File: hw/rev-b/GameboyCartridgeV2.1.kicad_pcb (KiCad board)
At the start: 6 copper layers, 52.8 x 61.2 mm, 148 parts, among them J1 USB_C_Receptacle_USB2.0, J2 Micro_SD_Card_Det2, J4 Conn_01x06, J5 CartBus, Q1 CJ2302, Q101 SIA975DJ-T1-GE3, Q102 2N7002, SW1 SW_Push, SW2 SW_Push, U1 USBLC6-2P6, U101 TPS2116DRLR, U102 TPS2553DBVR, U103 TPS63802DLAR, U104 ESP32-C3-MINI-1U-N4, U105 SN74LVC1G125DBVR, U106 SN74LVC3G34DCTR, U107 CH334P, U108 TLV3012BIDBVR, U109 TLV431BIDBZR, U2 W25Q16JVSSIQ, U3 RP2350_80QFN, U4 W956A8MBYA5I, U5 MCP79510, U6 AP2112K-3.3, U7 TXB0108PW, Y1 12MHz, Y101 12MHz 10pF 10ppm, Y2 32.768kHz

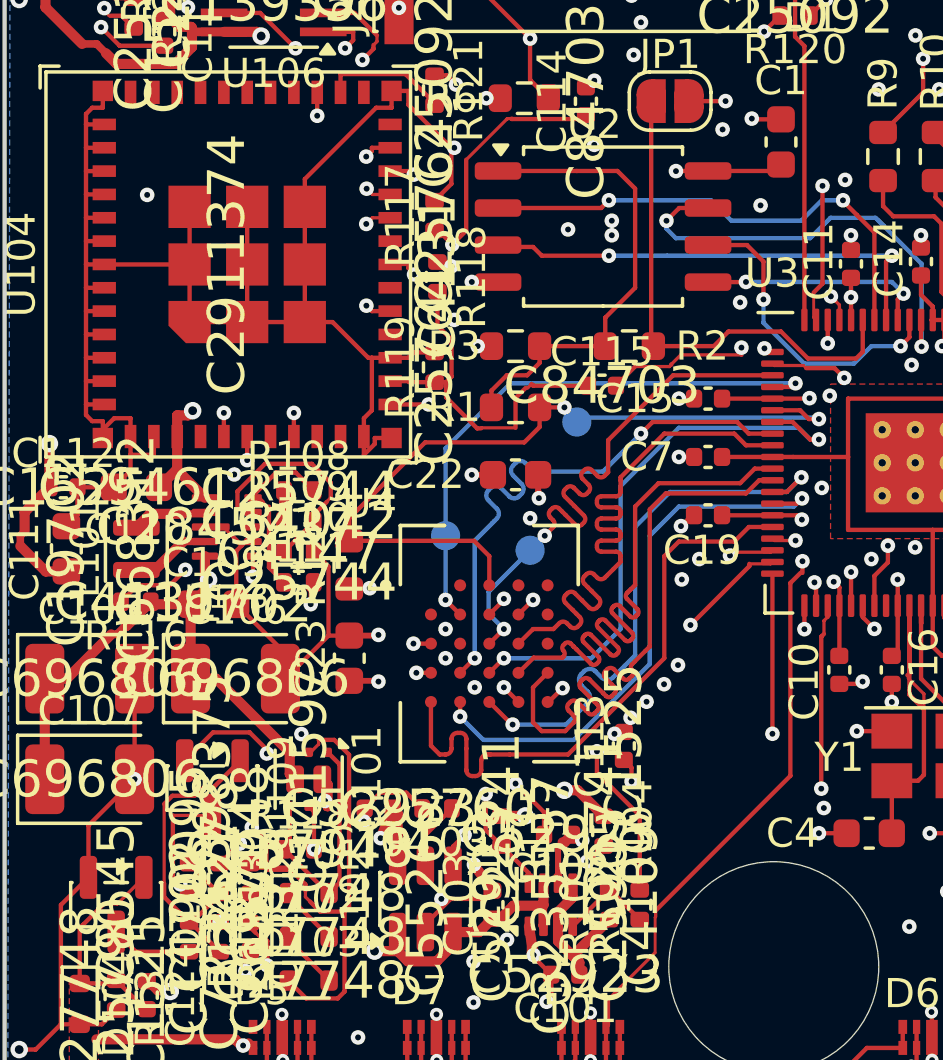
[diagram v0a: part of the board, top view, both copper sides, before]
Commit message: routing WIP: FB/PG resistor block re-arranged, USB_PWR_ST moved to ESP IO5 (pin 19), ADC_VCC divider moved to the VCC source; 5 open
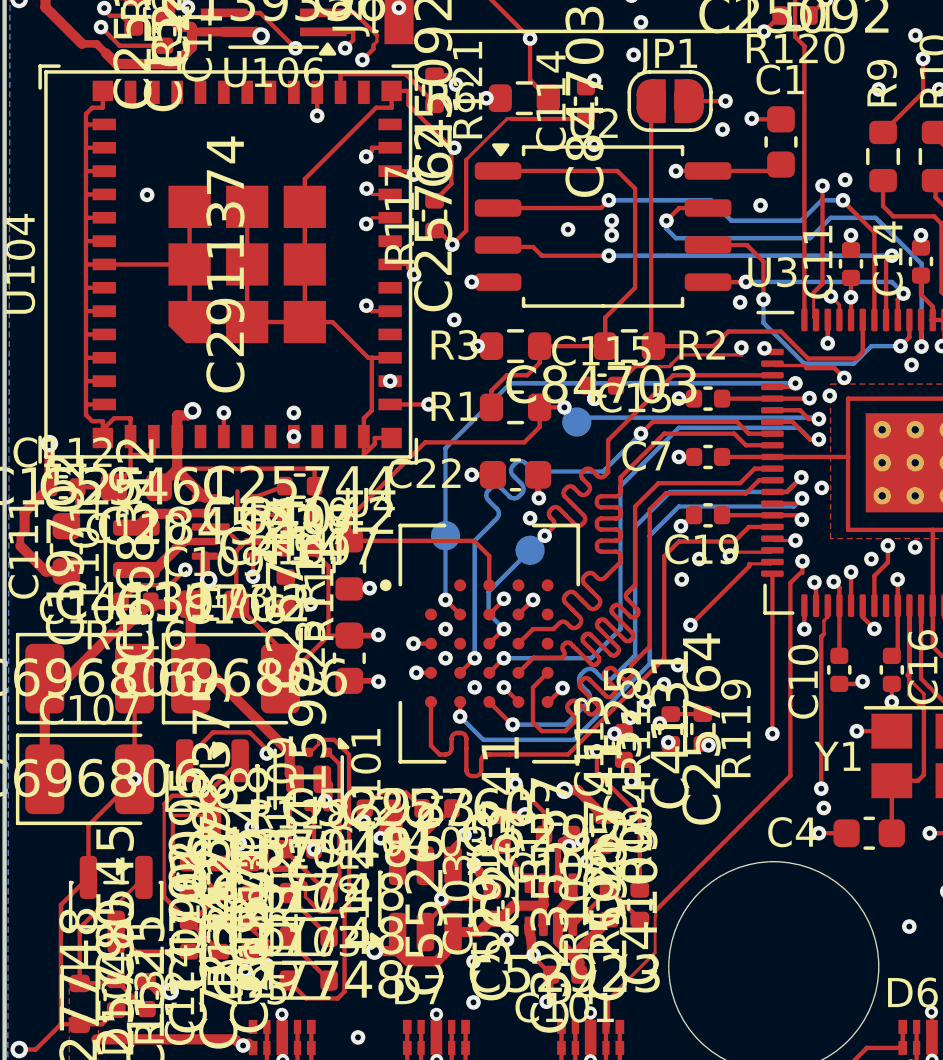
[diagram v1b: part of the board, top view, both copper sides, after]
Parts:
- moved R118 17.4 mm to (136.2, 99.9), turned to 90 degrees
- moved R119 15.4 mm to (137.3, 99.9), turned to -90 degrees
- moved R111 0.55 mm to (123.0, 95.2), turned to -90 degrees
- moved R108 0.15 mm to (123.5, 91.6), turned to 180 degrees
- moved R109 0.15 mm to (123.5, 92.7), turned to 180 degrees
- moved R110 0.15 mm to (123.5, 93.7)
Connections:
- U104 pad 19: unconnected-(U104-IO5-Pad19) -> /Radio/USB_PWR_ST
- U104 pad 6: /Radio/USB_PWR_ST -> unconnected-(U104-IO3-Pad6)
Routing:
- net VCC: track 77.6 -> 44.0 mm, vias 11 -> 10
- net /Radio/USB_PWR_ST: track 20.1 -> 1.58 mm, vias 2 -> 0
- net /Radio/ADC_VCC: track 12.4 -> 24.6 mm, vias 0 -> 4
- net /Radio/+3V3_RF: track 81.5 -> 86.8 mm
- net /Radio/RF_PG: track 6.22 -> 1.16 mm
- net /Radio/RF_FB: track 8.06 -> 3.28 mm
- net /Radio/ESP_EN: track 22.8 -> 21.2 mm
- net GND: track 229.7 -> 231.0 mm, vias 210 -> 212

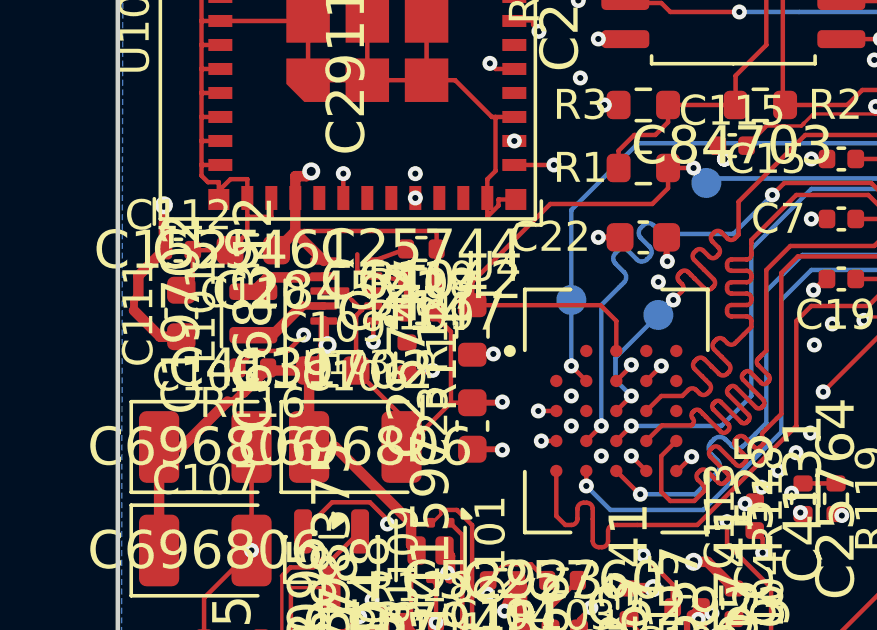
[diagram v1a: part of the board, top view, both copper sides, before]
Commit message: gate S1: full-system simulation with a Game Boy ROM (Peanut-GB + mailbox + RP2350/ESP models + shipped power manager + power plant), all pass; routing WIP; logbook
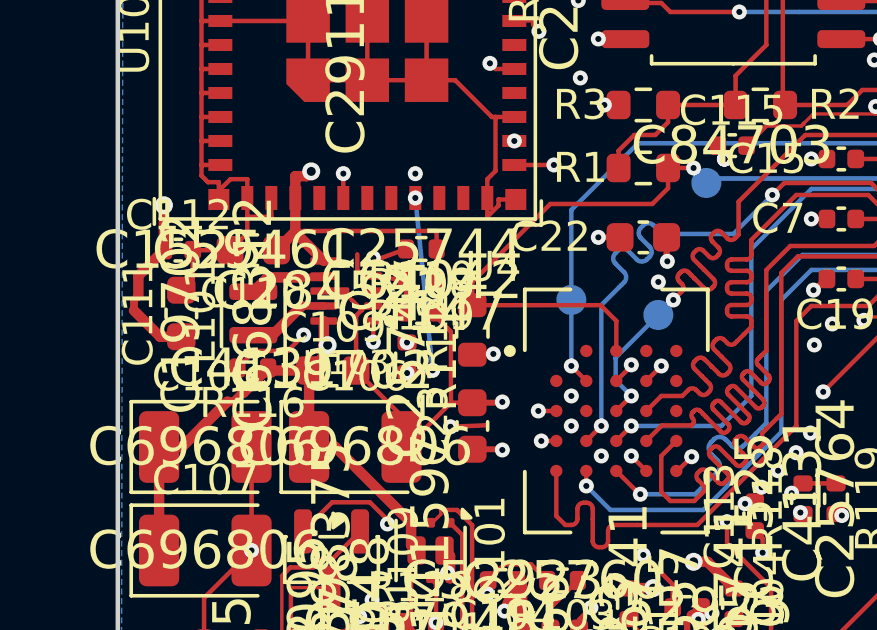
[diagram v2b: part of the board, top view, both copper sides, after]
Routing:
- net VRES: track 70.1 -> 59.7 mm
- net /Radio/RF_EN: track 34.0 -> 29.8 mm
- net /Radio/RF_PG: track 1.16 -> 4.54 mm, vias 0 -> 2
- net /Radio/ADC_VRES: track 29.1 -> 32.4 mm
- net /Radio/ESP_EN: track 21.2 -> 22.0 mm, vias 3 -> 5
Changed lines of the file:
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@@
-	)
-	(segment
-		(start 121.9 94.7042)
-		(end 123.6608 94.7042)
-		(width 0.15)
-		(layer "In2.Cu")
-		(net "/Radio/RF_EN")
 	)
 	(segment
@@
 	)
 	(segment
-		(start 123.6608 94.7042)
-		(end 125.4233 96.4667)
-		(width 0.15)
-		(layer "In2.Cu")
-		(net "/Radio/RF_EN")
-	)
-	(segment
 		(start 121.3662 92.3504)
 		(end 121.3662 91.7783)
@@
 		(width 0.15)
 		(layer "F.Cu")
+		(net "/Radio/RF_PG")
+	)
+	(segment
+		(start 121.9 92)
+		(end 121.9 91.9)
+		(width 0.15)
+		(layer "F.Cu")
+		(net "/Radio/RF_PG")
+	)
+	(via
+		(at 123.023038 94.715957)
+		(size 0.5)
+		(drill 0.2)
+		(layers "F.Cu" "B.Cu")
+		(net "/Radio/RF_PG")
+	)
+	(via
+		(at 121.9 91.9)
+		(size 0.5)
+		(drill 0.2)
+		(layers "F.Cu" "B.Cu")
+		(net "/Radio/RF_PG")
+	)
+	(segment
+		(start 121.9 91.9)
+		(end 123.008038 93.000958)
+		(width 0.15)
+		(layer "In2.Cu")
+		(net "/Radio/RF_PG")
+	)
+	(segment
+		(start 123.008038 93.000958)
+		(end 123.023038 94.715957)
+		(width 0.15)
+		(layer "In2.Cu")
 		(net "/Radio/RF_PG")
 	)
@@
 	)
 	(segment
-		(start 131.4952 94.1211)
-		(end 121.0635 94.1211)
-		(width 0.35)
-		(layer "In2.Cu")
-		(net "VRES")
-	)
-	(segment
 		(start 144.3197 95.3752)
 		(end 144.1731 95.3752)
@@
 	)
 	(segment
+		(start 125.6715 97.4767)
+		(end 124.472552 97.52695)
+		(width 0.15)
+		(layer "F.Cu")
+		(net "/Radio/ESP_EN")
+	)
+	(segment
 		(start 134.8764 101.723)
 		(end 134.8764 101.2494)
 		(width 0.15)
 		(layer "F.Cu")
+		(net "/Radio/ESP_EN")
+	)
+	(via
+		(at 123.023038 95.735957)
+		(size 0.5)
+		(drill 0.2)
+		(layers "F.Cu" "B.Cu")
 		(net "/Radio/ESP_EN")
 	)
@@
 	)
 	(via
+		(at 124.472552 97.52695)
+		(size 0.5)
+		(drill 0.2)
+		(layers "F.Cu" "B.Cu")
+		(net "/Radio/ESP_EN")
+	)
+	(via
 		(at 134.8764 101.723)
 		(size 0.5)
@@
 	)
 	(segment
-		(start 123.877 95.6822)
-		(end 125.6715 97.4767)
-		(width 0.15)
-		(layer "In2.Cu")
+		(start 123.3 89.9)
+		(end 123.877 95.6472)
+		(width 0.15)
+		(layer "B.Cu")
 		(net "/Radio/ESP_EN")
 	)
@@
 	)
 	(segment
+		(start 124.458038 97.200958)
+		(end 124.472552 97.52695)
+		(width 0.15)
+		(layer "In2.Cu")
+		(net "/Radio/ESP_EN")
+	)
+	(segment
 		(start 129.789 101.1677)
 		(end 134.3211 101.1677)
@@
 	)
 	(segment
-		(start 123.877 95.6472)
-		(end 123.877 95.6822)
-		(width 0.15)
-		(layer "In2.Cu")
-		(net "/Radio/ESP_EN")
-	)
-	(segment
 		(start 125.6715 97.4767)
 		(end 126.098 97.4767)
@@
 	)
 	(segment
+		(start 123.023038 95.735957)
+		(end 124.458038 97.200958)
+		(width 0.15)
+		(layer "In2.Cu")
+		(net "/Radio/ESP_EN")
+	)
+	(segment
 		(start 126.098 97.4767)
 		(end 129.789 101.1677)
 		(width 0.15)
 		(layer "In2.Cu")
-		(net "/Radio/ESP_EN")
-	)
-	(segment
-		(start 123.877 95.6472)
-		(end 123.308038 95.100957)
-		(width 0.15)
-		(layer "In3.Cu")
-		(net "/Radio/ESP_EN")
-	)
-	(segment
-		(start 123.308038 95.100957)
-		(end 123.3 89.9)
-		(width 0.15)
-		(layer "In3.Cu")
 		(net "/Radio/ESP_EN")
 	)
@@
 	)
 	(segment
-		(start 125.2468 88.8)
+		(start 127.919 88.8)
+		(end 125.358038 91.350957)
+		(width 0.15)
+		(layer "In2.Cu")
+		(net "/Radio/ADC_VRES")
+	)
+	(segment
+		(start 125.358038 91.350957)
+		(end 121.758038 91.350957)
+		(width 0.15)
+		(layer "In2.Cu")
+		(net "/Radio/ADC_VRES")
+	)
+	(segment
+		(start 121.658037 91.400958)
+		(end 121.558038 91.500958)
+		(width 0.15)
+		(layer "In2.Cu")
+		(net "/Radio/ADC_VRES")
+	)
+	(segment
+		(start 119.558038 93.450958)
 		(end 119.5777 94.4691)
 		(width 0.15)
@@
 		(width 0.15)
 		(layer "In2.Cu")
+		(net "/Radio/ADC_VRES")
+	)
+	(segment
+		(start 121.758038 91.350957)
+		(end 121.708038 91.400958)
+		(width 0.15)
+		(layer "In2.Cu")
+		(net "/Radio/ADC_VRES")
+	)
+	(segment
+		(start 121.508038 91.500958)
+		(end 119.558038 93.450958)
+		(width 0.15)
+		(layer "In2.Cu")
+		(net "/Radio/ADC_VRES")
+	)
+	(segment
+		(start 121.558038 91.500958)
+		(end 121.508038 91.500958)
+		(width 0.15)
+		(layer "In2.Cu")
+		(net "/Radio/ADC_VRES")
+	)
+	(segment
+		(start 121.708038 91.400958)
+		(end 121.658037 91.400958)
+		(width 0.15)
+		(layer "In2.Cu")

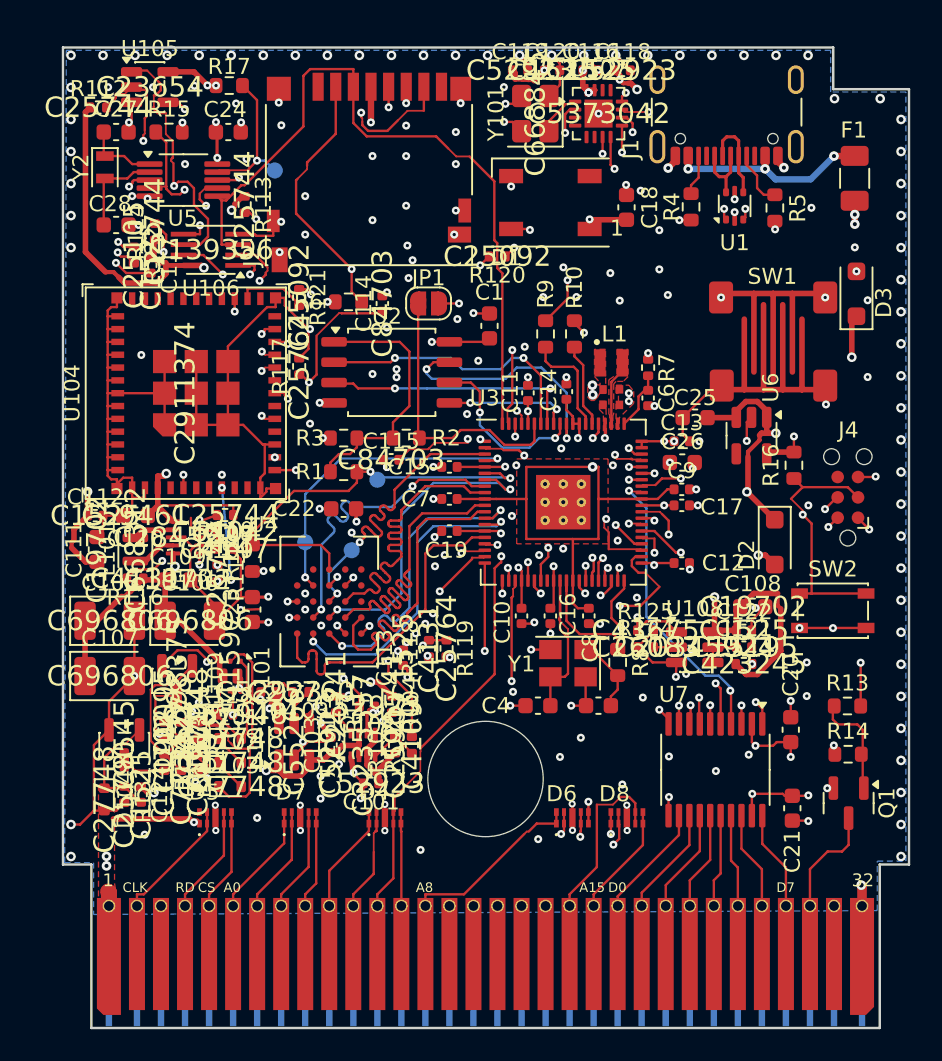
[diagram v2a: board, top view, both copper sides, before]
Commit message: design calcs: USB_PWR_ST on ESP IO5 (pin 19)
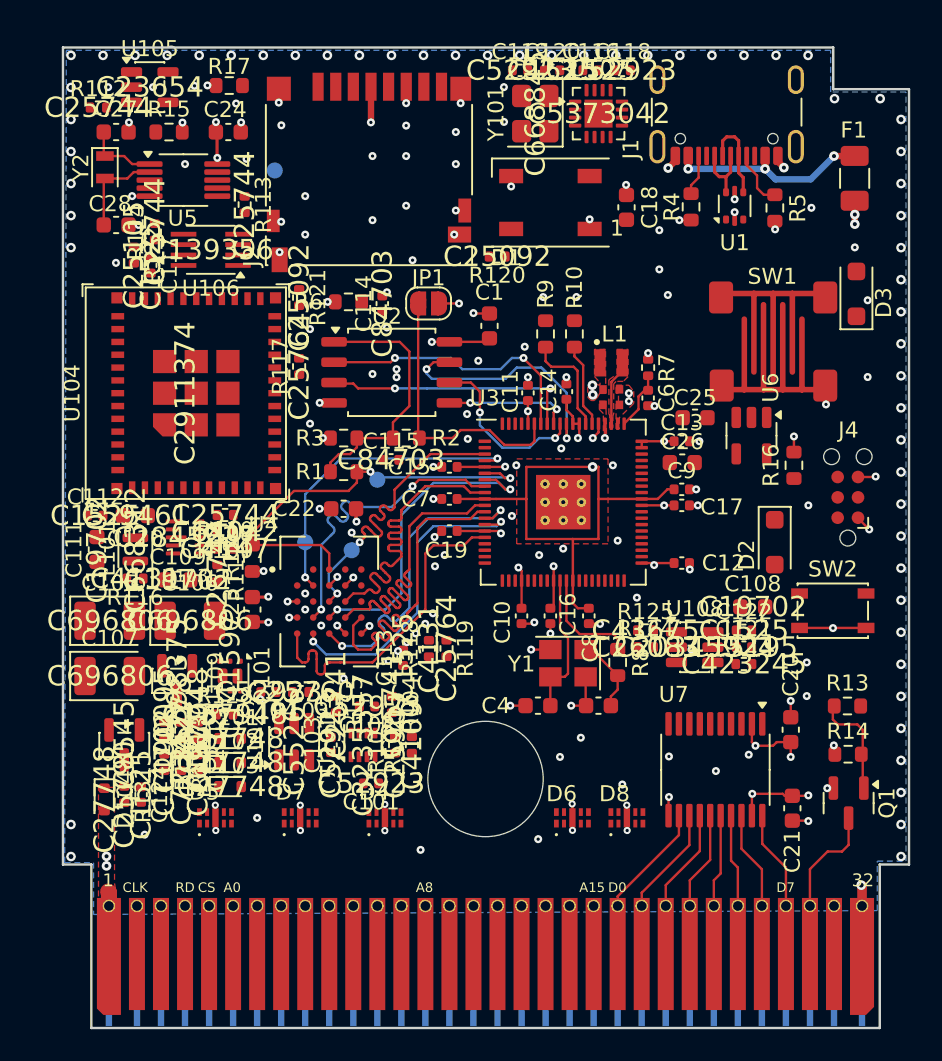
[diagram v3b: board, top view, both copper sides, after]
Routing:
- net GND: track 231.0 -> 49.0 mm, vias 212 -> 194
- net /Radio/+3V3_RF: track 86.8 -> 0.00 mm, vias 6 -> 0
- net VRES: track 59.7 -> 0.00 mm, vias 2 -> 0
- net DEBUG_UART_TX: track 58.9 -> 0.00 mm, vias 3 -> 0
- net SPI_MISO: track 51.9 -> 0.00 mm, vias 4 -> 0
- net GB_CLK: track 46.8 -> 0.00 mm, vias 1 -> 0
- net SPI_MOSI: track 46.6 -> 0.00 mm
- net SPI_CLK: track 45.9 -> 0.00 mm, vias 4 -> 0
- net RTC_CS: track 43.9 -> 0.00 mm, vias 2 -> 0
- net GB_A14: track 41.9 -> 0.00 mm, vias 1 -> 0
- net GB_A8: track 41.6 -> 0.00 mm, vias 1 -> 0
- net VCC: track 44.0 -> 5.86 mm, vias 10 -> 4
- net GB_RD: track 37.6 -> 0.00 mm, vias 1 -> 0
- net GB_A15: track 36.8 -> 0.00 mm, vias 1 -> 0
- net GB_CS: track 35.8 -> 0.00 mm, vias 1 -> 0
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
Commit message: routing: clean re-route from the placement state (Freerouting x2): 27 open
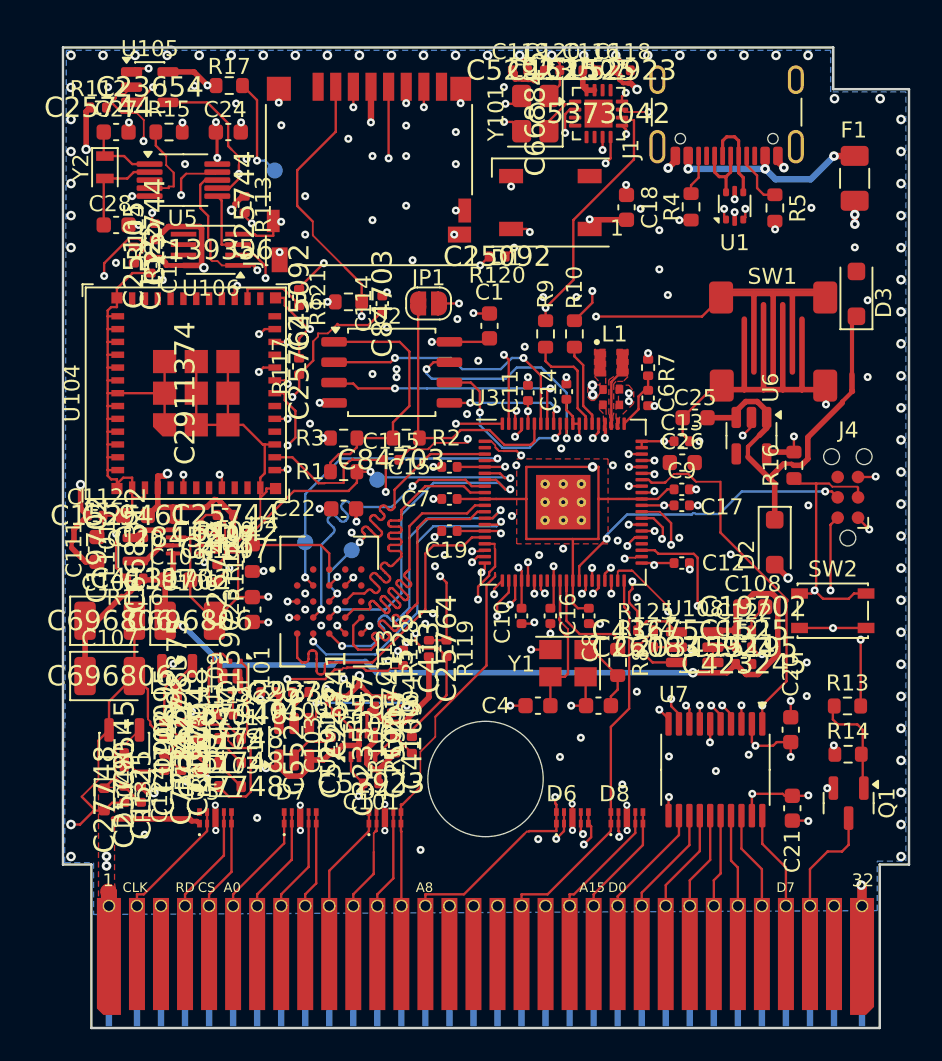
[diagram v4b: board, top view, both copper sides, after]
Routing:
- net GND: track 49.0 -> 201.1 mm, vias 194 -> 197
- net /Radio/+3V3_RF: track 0.00 -> 89.5 mm, vias 0 -> 6
- net VRES: track 0.00 -> 65.1 mm, vias 0 -> 2
- net DEBUG_UART_TX: track 0.00 -> 50.4 mm, vias 0 -> 2
- net SPI_MISO: track 0.00 -> 48.1 mm, vias 0 -> 3
- net SPI_CLK: track 0.00 -> 42.9 mm, vias 0 -> 3
- net GB_CLK: track 0.00 -> 42.0 mm, vias 0 -> 1
- net GB_RD: track 0.00 -> 37.2 mm, vias 0 -> 1
- net GB_A14: track 0.00 -> 36.7 mm, vias 0 -> 1
- net /Radio/ADC_VRES: track 0.00 -> 36.4 mm, vias 0 -> 3
- net GB_CS: track 0.00 -> 35.6 mm, vias 0 -> 1
- net GB_A0: track 0.00 -> 35.3 mm, vias 0 -> 1
- net GB_A4: track 0.00 -> 34.6 mm, vias 0 -> 1
- net /Radio/RF_EN: track 0.00 -> 34.4 mm, vias 0 -> 2
- net GB_A3: track 0.00 -> 33.8 mm, vias 0 -> 1
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
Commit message: routing: finisher enforces hole-to-hole for new vias; BUTTON re-routed clear of SW1; 7 open, no new copper DRC errors except one VRES via pair
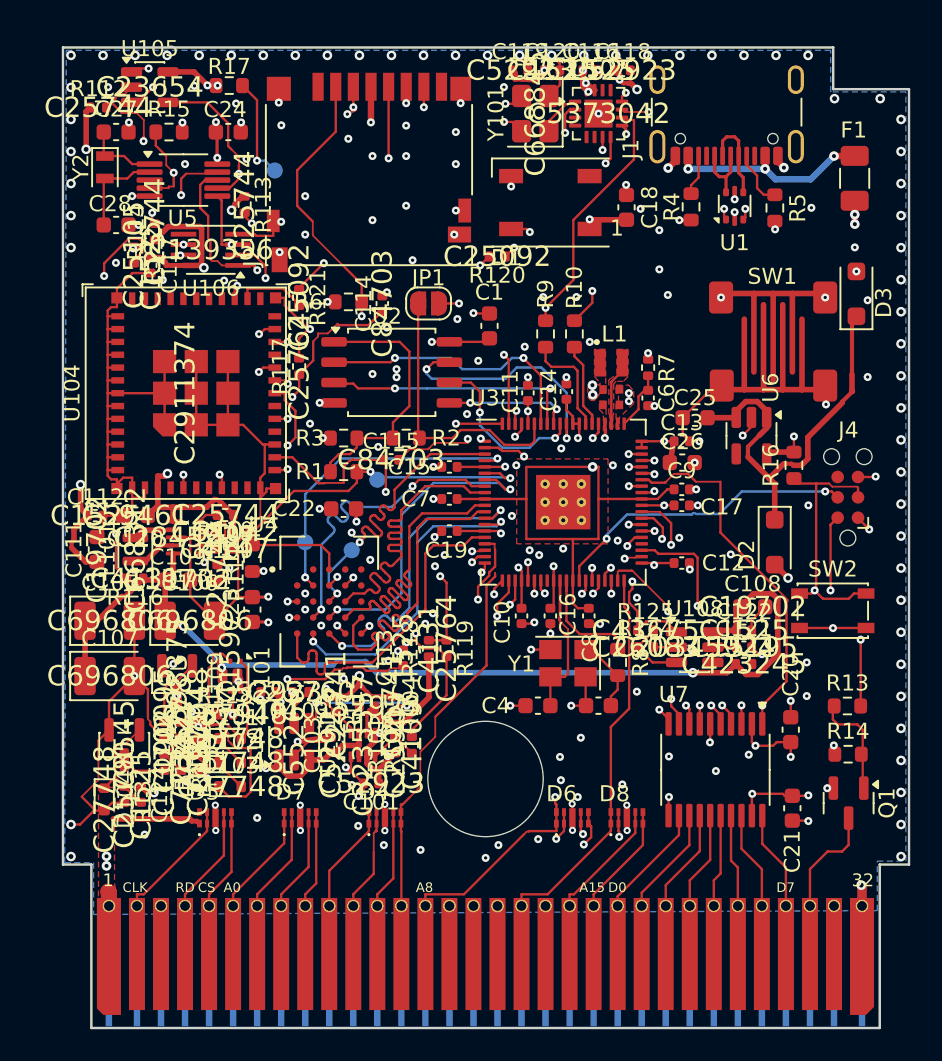
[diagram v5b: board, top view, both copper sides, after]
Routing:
- net GND: track 201.1 -> 274.5 mm, vias 197 -> 212
- net VBUS: track 7.31 -> 79.7 mm, vias 3 -> 8
- net RTC_CS: track 5.47 -> 44.2 mm, vias 0 -> 3
- net +3V3: track 59.9 -> 77.4 mm, vias 32 -> 38
- net SPI_MOSI: track 30.7 -> 42.9 mm, vias 2 -> 4
- net VLIM: track 3.03 -> 7.10 mm, vias 0 -> 2
- net /Radio/REG_G: track 16.7 -> 20.5 mm, vias 0 -> 2
- net DEBUG_UART_TX: track 50.4 -> 54.1 mm, vias 2 -> 4
- net /Radio/ESP_SCK_BUF: track 0.00 -> 3.43 mm, vias 0 -> 2
- net /Radio/VMUX: track 17.8 -> 20.9 mm, vias 2 -> 3
- net BUTTON: track 29.8 -> 27.2 mm, vias 2 -> 4
- net VRES: track 65.1 -> 65.8 mm, vias 2 -> 4
